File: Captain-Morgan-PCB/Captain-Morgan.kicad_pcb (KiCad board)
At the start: 2 copper layers, 56 x 65 mm, 130 parts, among them J1 RPi_GPIO, J2 MMCX_H, J3 PINHEADER_2X2_SMD, J4 PINHEADER_2X2_SMD, P1 BATT, U1 A2200-A, U2 Racom R-78B5.0-1.5L

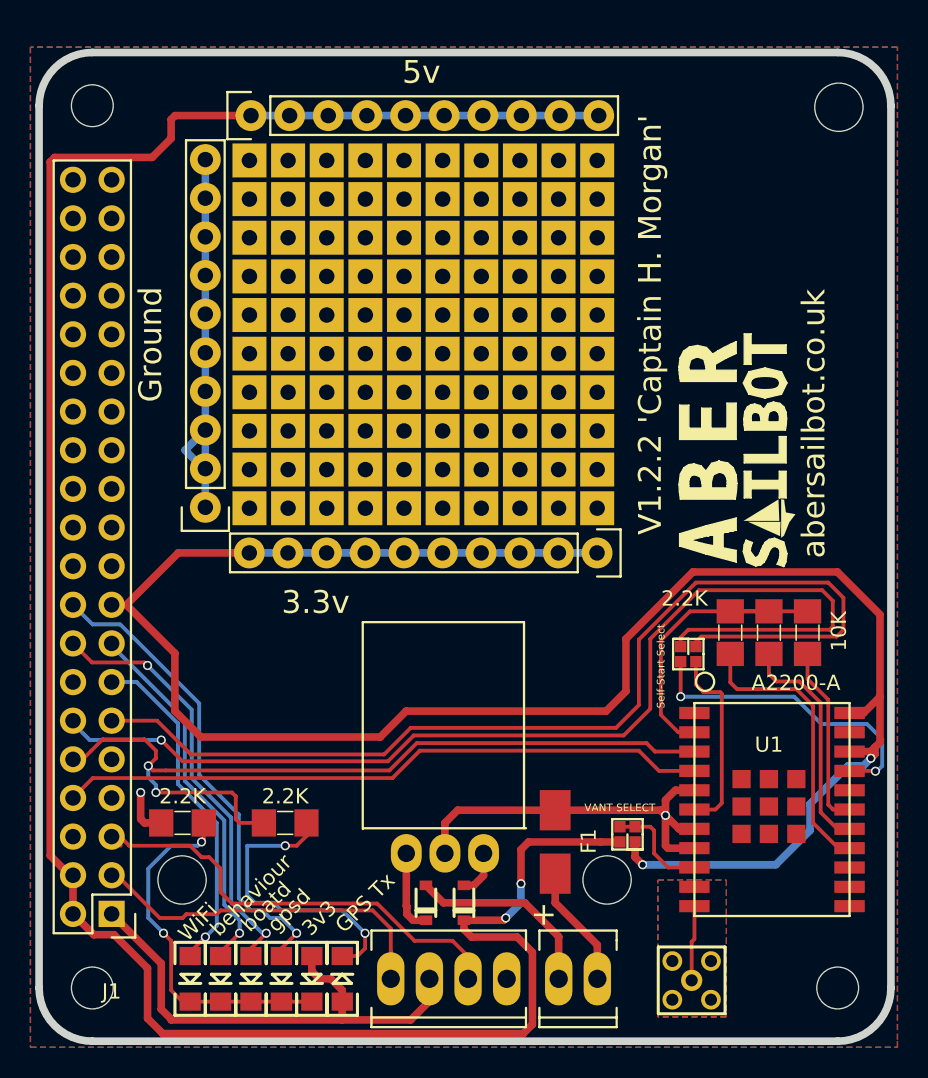
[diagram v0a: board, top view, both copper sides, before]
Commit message: Removed filled zone, arduino footprint and proto area.
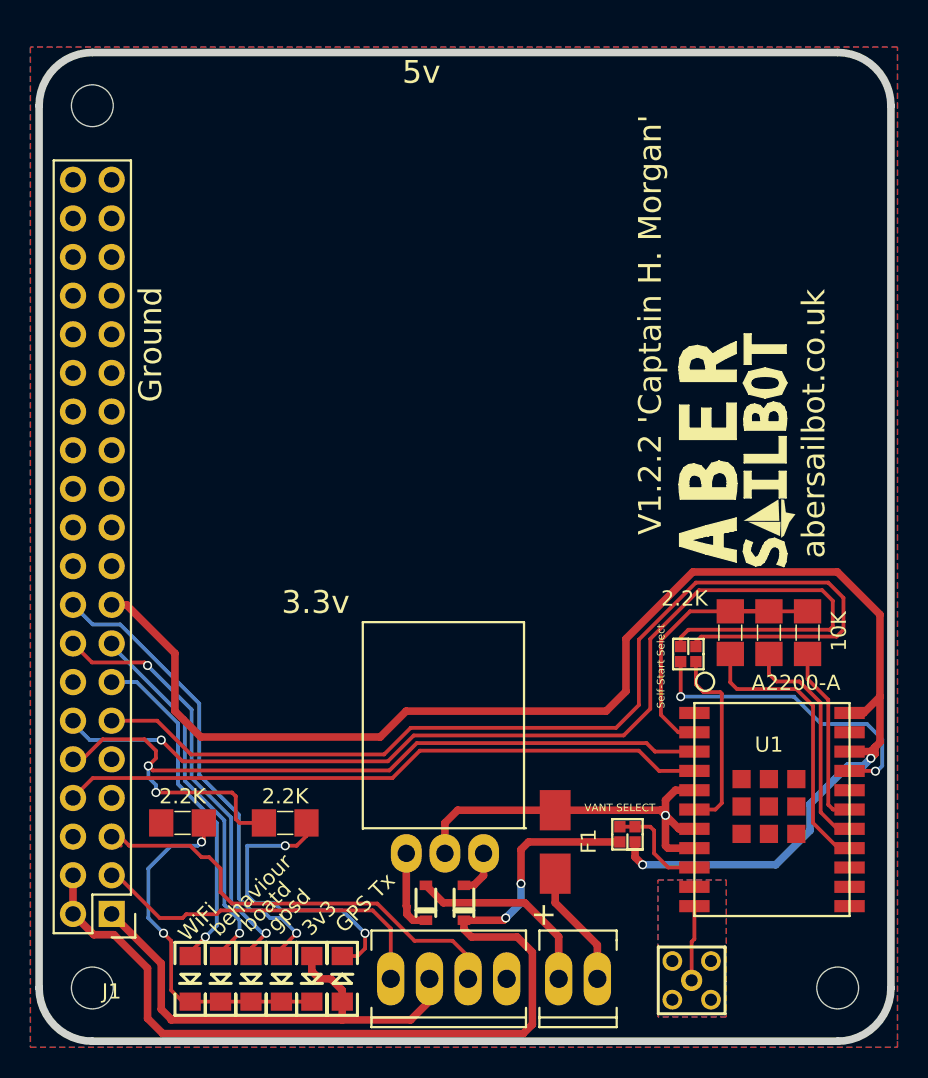
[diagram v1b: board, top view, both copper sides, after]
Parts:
- removed ARDUINO_SHIELD: val**, Sailbot_Custom:ARDUINO_SHIELD_3_HOLE
- removed REF**11 (x3): Pin_Header_Straight_1x10, Pin_Headers:Pin_Header_Straight_1x10
- removed REF**1111101, REF**11111010, REF**1111102, REF**1111103, REF**1111104, REF**1111105, REF**1111106, REF**1111107, REF**1111108, REF**1111109, REF**111111, REF**1111110, REF**111112, REF**111113, REF**111114, REF**111115, REF**111116, REF**111117, REF**111118, REF**111119, REF**111121, REF**1111210, REF**111122, REF**111123, REF**111124, REF**111125, REF**111126, REF**111127, REF**111128, REF**111129, REF**111131, REF**1111310, REF**111132, REF**111133, REF**111134, REF**111135, REF**111136, REF**111137, REF**111138, REF**111139, REF**111141, REF**1111410, REF**111142, REF**111143, REF**111144, REF**111145, REF**111146, REF**111147, REF**111148, REF**111149, REF**111151, REF**1111510, REF**111152, REF**111153, REF**111154, REF**111155, REF**111156, REF**111157, REF**111158, REF**111159, REF**111161, REF**1111610, REF**111162, REF**111163, REF**111164, REF**111165, REF**111166, REF**111167, REF**111168, REF**111169, REF**111171, REF**1111710, REF**111172, REF**111173, REF**111174, REF**111175, REF**111176, REF**111177, REF**111178, REF**111179, REF**111181, REF**1111810, REF**111182, REF**111183, REF**111184, REF**111185, REF**111186, REF**111187, REF**111188, REF**111189, REF**111191, REF**1111910, REF**111192, REF**111193, REF**111194, REF**111195, REF**111196, REF**111197, REF**111198, REF**111199: Pin_Header_Straight_1x01, Sailbot_Custom:Pin_Header_Straight_1x01
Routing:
- net +5V: track 149.7 -> 64.1 mm
- net +3V3: track 165.4 -> 133.0 mm
- net GND: track 57.4 -> 27.6 mm, vias 2 -> 1
